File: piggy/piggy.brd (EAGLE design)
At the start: 91.8 x 23 mm, 7 parts, among them J1 M05X2PTH

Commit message: aligned jacks to pot origin
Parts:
- moved CV_JACK 2.54 mm to (39.4, 8.89), turned to 180 degrees
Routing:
- net N$1: track 9.55 -> 14.7 mm
- net LIN: track 84.2 -> 79.5 mm
- net CV_PANEL: track 60.3 -> 62.7 mm
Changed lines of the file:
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@@
 <element name="J1" library="SparkFun" package="AVR_ICSP" value="M05X2PTH" x="81.28" y="19.05" rot="R90"/>
 <element name="IN_JACK" library="erthenvar" package="ERTHENVAR-JACK" value="AUDIO-JACKERTHENVAR" x="71.12" y="8.89" rot="R180"/>
-<element name="CV_JACK" library="erthenvar" package="ERTHENVAR-JACK" value="AUDIO-JACKERTHENVAR" x="39.37" y="6.35"/>
+<element name="CV_JACK" library="erthenvar" package="ERTHENVAR-JACK" value="AUDIO-JACKERTHENVAR" x="39.37" y="8.89" rot="R180"/>
 <element name="OUT_JACK" library="erthenvar" package="ERTHENVAR-JACK" value="AUDIO-JACKERTHENVAR" x="83.82" y="8.89" rot="R180"/>
 <element name="P_GAIN" library="SparkFun" package="PDB12" value="100KB" x="58.42" y="8.89" rot="R90"/>
@@
 <contactref element="J1" pad="9"/>
 <contactref element="P_CV" pad="2"/>
-<wire x1="30.4" y1="8.89" x2="54.356" y2="8.89" width="0.254" layer="1"/>
 <wire x1="54.356" y1="8.89" x2="61.468" y2="15.748" width="0.254" layer="1"/>
 <wire x1="61.468" y1="15.748" x2="72.898" y2="15.748" width="0.254" layer="1"/>
@@
 <wire x1="74.168" y1="14.732" x2="83.312" y2="14.732" width="0.254" layer="16"/>
 <wire x1="83.312" y1="14.732" x2="86.36" y2="17.78" width="0.254" layer="16"/>
+<wire x1="30.4" y1="8.89" x2="32.004" y2="8.89" width="0.254" layer="1"/>
+<wire x1="32.004" y1="8.89" x2="34.036" y2="6.858" width="0.254" layer="1"/>
+<wire x1="34.036" y1="6.858" x2="42.164" y2="6.858" width="0.254" layer="1"/>
+<wire x1="42.164" y1="6.858" x2="42.926" y2="6.096" width="0.254" layer="1"/>
+<wire x1="42.926" y1="6.096" x2="48.006" y2="6.096" width="0.254" layer="1"/>
+<wire x1="48.006" y1="6.096" x2="50.8" y2="8.89" width="0.254" layer="1"/>
+<wire x1="50.8" y1="8.89" x2="54.356" y2="8.89" width="0.254" layer="1"/>
 </signal>
 <signal name="GAIN">
@@
 <contactref element="U$1" pad="X1"/>
 <contactref element="U$1" pad="X2"/>
-<wire x1="6.32" y1="7.33" x2="8.92" y2="7.33" width="0.4064" layer="1"/>
-<wire x1="78.74" y1="20.32" x2="78.74" y2="20.574" width="0.4064" layer="16"/>
-<wire x1="78.74" y1="20.574" x2="77.724" y2="21.59" width="0.254" layer="16"/>
-<wire x1="77.724" y1="21.59" x2="71.374" y2="21.59" width="0.254" layer="16"/>
-<wire x1="71.374" y1="21.59" x2="65.024" y2="15.24" width="0.254" layer="16"/>
-<wire x1="65.024" y1="15.24" x2="65.024" y2="11.684" width="0.254" layer="16"/>
-<wire x1="65.024" y1="11.684" x2="63.754" y2="10.414" width="0.254" layer="16"/>
-<wire x1="63.754" y1="10.414" x2="43.942" y2="10.414" width="0.254" layer="16"/>
-<wire x1="43.942" y1="10.414" x2="40.132" y2="14.224" width="0.254" layer="16"/>
-<wire x1="40.132" y1="14.224" x2="27.178" y2="14.224" width="0.254" layer="16"/>
-<wire x1="27.178" y1="14.224" x2="20.32" y2="7.366" width="0.254" layer="16"/>
-<wire x1="20.32" y1="7.366" x2="8.956" y2="7.366" width="0.254" layer="16"/>
-<wire x1="8.956" y1="7.366" x2="8.92" y2="7.33" width="0.254" layer="16"/>
+<wire x1="6.32" y1="7.33" x2="8.382" y2="7.33" width="0.4064" layer="1"/>
+<wire x1="8.382" y1="7.33" x2="8.92" y2="7.33" width="0.4064" layer="1"/>
+<wire x1="78.74" y1="20.32" x2="78.74" y2="20.574" width="0.254" layer="1"/>
+<wire x1="78.74" y1="20.574" x2="77.724" y2="21.59" width="0.254" layer="1"/>
+<wire x1="77.724" y1="21.59" x2="34.798" y2="21.59" width="0.254" layer="1"/>
+<wire x1="34.798" y1="21.59" x2="20.574" y2="7.366" width="0.254" layer="1"/>
+<wire x1="20.574" y1="7.366" x2="8.418" y2="7.366" width="0.254" layer="1"/>
+<wire x1="8.418" y1="7.366" x2="8.382" y2="7.33" width="0.254" layer="1"/>
 </signal>
 <signal name="EXP">
@@
 <contactref element="CV_JACK" pad="3"/>
 <contactref element="P_CV" pad="3"/>
-<wire x1="30.4" y1="12.64" x2="37.98" y2="12.64" width="0.4064" layer="1"/>
-<wire x1="37.98" y1="12.64" x2="39.37" y2="11.25" width="0.4064" layer="1"/>
+<wire x1="39.37" y1="3.99" x2="39.37" y2="7.62" width="0.254" layer="16"/>
+<wire x1="39.37" y1="7.62" x2="34.29" y2="12.7" width="0.254" layer="16"/>
+<wire x1="34.29" y1="12.7" x2="30.46" y2="12.7" width="0.254" layer="16"/>
+<wire x1="30.46" y1="12.7" x2="30.4" y2="12.64" width="0.254" layer="16"/>
 </signal>
 </signals>

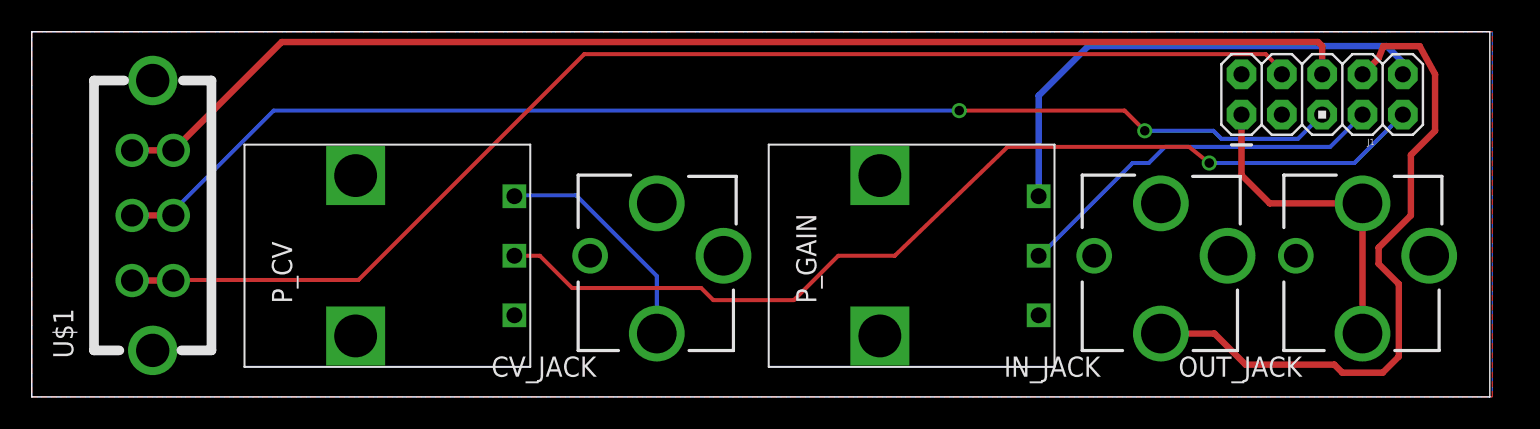
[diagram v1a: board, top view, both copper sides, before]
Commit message: Laid out panel.
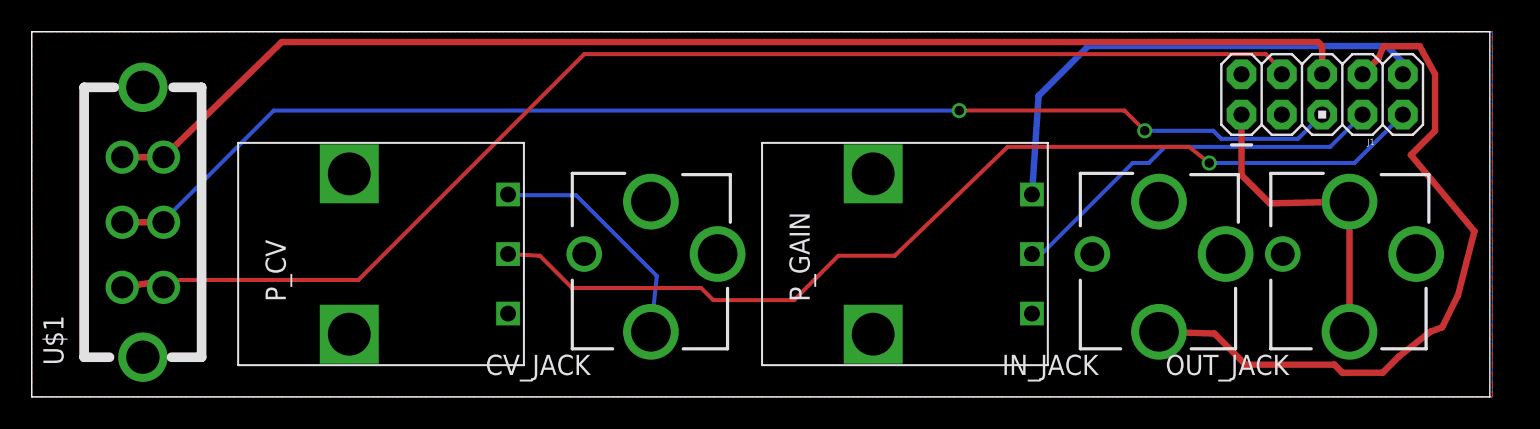
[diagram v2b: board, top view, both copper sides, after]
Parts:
- moved OUT_JACK 0.83 mm to (83.0, 9.00)
- moved U$1 0.75 mm to (7.00, 11.0)
- moved P_GAIN 0.43 mm to (58.0, 9.00)
- moved P_CV 0.41 mm to (25.0, 9.00)
- moved CV_JACK 0.39 mm to (39.0, 9.00)
- moved IN_JACK 0.16 mm to (71.0, 9.00)
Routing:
- net IN: track 42.8 -> 44.8 mm
- net OUT: track 20.4 -> 19.5 mm
- net EXP: track 79.7 -> 80.4 mm
- net INT: track 79.2 -> 79.9 mm
- net LIN: track 79.5 -> 80.1 mm
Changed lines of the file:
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@@
 <setting verticaltext="up"/>
 </settings>
-<grid distance="0.01" unitdist="inch" unit="inch" style="lines" multiple="1" display="yes" altdistance="0.005" altunitdist="inch" altunit="inch"/>
+<grid distance="1" unitdist="mm" unit="mm" style="lines" multiple="1" display="yes" altdistance="0.1" altunitdist="mm" altunit="mm"/>
 <layers>
 <layer number="1" name="Top" color="4" fill="1" visible="yes" active="yes"/>
@@
 <elements>
 <element name="J1" library="SparkFun" package="AVR_ICSP" value="M05X2PTH" x="81.28" y="19.05" rot="R90"/>
-<element name="IN_JACK" library="erthenvar" package="ERTHENVAR-JACK" value="AUDIO-JACKERTHENVAR" x="71.12" y="8.89" rot="R180"/>
-<element name="CV_JACK" library="erthenvar" package="ERTHENVAR-JACK" value="AUDIO-JACKERTHENVAR" x="39.37" y="8.89" rot="R180"/>
-<element name="OUT_JACK" library="erthenvar" package="ERTHENVAR-JACK" value="AUDIO-JACKERTHENVAR" x="83.82" y="8.89" rot="R180"/>
-<element name="P_GAIN" library="SparkFun" package="PDB12" value="100KB" x="58.42" y="8.89" rot="R90"/>
-<element name="P_CV" library="SparkFun" package="PDB12" value="100KB" x="25.4" y="8.89" rot="R90"/>
-<element name="U$1" library="russruss" package="MOUNTAIN_10SL005" value="DPDT" x="7.62" y="11.43" rot="R90"/>
+<element name="IN_JACK" library="erthenvar" package="ERTHENVAR-JACK" value="AUDIO-JACKERTHENVAR" x="71" y="9" rot="R180"/>
+<element name="CV_JACK" library="erthenvar" package="ERTHENVAR-JACK" value="AUDIO-JACKERTHENVAR" x="39" y="9" rot="R180"/>
+<element name="OUT_JACK" library="erthenvar" package="ERTHENVAR-JACK" value="AUDIO-JACKERTHENVAR" x="83" y="9" rot="R180"/>
+<element name="P_GAIN" library="SparkFun" package="PDB12" value="100KB" x="58" y="9" rot="R90"/>
+<element name="P_CV" library="SparkFun" package="PDB12" value="100KB" x="25" y="9" rot="R90"/>
+<element name="U$1" library="russruss" package="MOUNTAIN_10SL005" value="DPDT" x="7" y="11" rot="R90"/>
 </elements>
 <signals>
@@
 <contactref element="J1" pad="10"/>
 <contactref element="P_GAIN" pad="3"/>
-<wire x1="63.42" y1="12.64" x2="63.42" y2="18.97" width="0.4064" layer="16"/>
+<wire x1="63" y1="12.75" x2="63.42" y2="18.97" width="0.4064" layer="16"/>
 <wire x1="63.42" y1="18.97" x2="66.548" y2="22.098" width="0.4064" layer="16"/>
 <wire x1="66.548" y1="22.098" x2="85.344" y2="22.098" width="0.4064" layer="16"/>
@@
 <wire x1="74.168" y1="14.732" x2="83.312" y2="14.732" width="0.254" layer="16"/>
 <wire x1="83.312" y1="14.732" x2="86.36" y2="17.78" width="0.254" layer="16"/>
-<wire x1="30.4" y1="8.89" x2="32.004" y2="8.89" width="0.254" layer="1"/>
+<wire x1="30" y1="9" x2="32.004" y2="8.89" width="0.254" layer="1"/>
 <wire x1="32.004" y1="8.89" x2="34.036" y2="6.858" width="0.254" layer="1"/>
 <wire x1="34.036" y1="6.858" x2="42.164" y2="6.858" width="0.254" layer="1"/>
@@
 <contactref element="J1" pad="7"/>
 <contactref element="P_GAIN" pad="2"/>
-<wire x1="63.42" y1="8.89" x2="63.5" y2="8.89" width="0.254" layer="16"/>
+<wire x1="63" y1="9" x2="63.5" y2="8.89" width="0.254" layer="16"/>
 <wire x1="63.5" y1="8.89" x2="69.342" y2="14.732" width="0.254" layer="16"/>
 <wire x1="69.342" y1="14.732" x2="70.358" y2="14.732" width="0.254" layer="16"/>
@@
 <contactref element="U$1" pad="X1"/>
 <contactref element="U$1" pad="X2"/>
-<wire x1="6.32" y1="7.33" x2="8.382" y2="7.33" width="0.4064" layer="1"/>
-<wire x1="8.382" y1="7.33" x2="8.92" y2="7.33" width="0.4064" layer="1"/>
+<wire x1="5.7" y1="6.9" x2="8.382" y2="7.33" width="0.4064" layer="1"/>
+<wire x1="8.382" y1="7.33" x2="8.3" y2="6.9" width="0.4064" layer="1"/>
 <wire x1="78.74" y1="20.32" x2="78.74" y2="20.574" width="0.254" layer="1"/>
 <wire x1="78.74" y1="20.574" x2="77.724" y2="21.59" width="0.254" layer="1"/>
@@
 <contactref element="U$1" pad="Y1"/>
 <contactref element="U$1" pad="Y2"/>
-<wire x1="6.32" y1="15.53" x2="8.92" y2="15.53" width="0.4064" layer="1"/>
+<wire x1="5.7" y1="15.1" x2="8.3" y2="15.1" width="0.4064" layer="1"/>
 <wire x1="81.28" y1="20.32" x2="81.28" y2="22.098" width="0.4064" layer="1"/>
 <wire x1="81.28" y1="22.098" x2="81.026" y2="22.352" width="0.4064" layer="1"/>
 <wire x1="81.026" y1="22.352" x2="15.742" y2="22.352" width="0.4064" layer="1"/>
-<wire x1="15.742" y1="22.352" x2="8.92" y2="15.53" width="0.4064" layer="1"/>
+<wire x1="15.742" y1="22.352" x2="8.3" y2="15.1" width="0.4064" layer="1"/>
 </signal>
 <signal name="IN">
 <contactref element="J1" pad="8"/>
 <contactref element="IN_JACK" pad="3"/>
-<wire x1="71.12" y1="3.99" x2="74.496" y2="3.99" width="0.4064" layer="1"/>
+<wire x1="71" y1="4.1" x2="74.496" y2="3.99" width="0.4064" layer="1"/>
 <wire x1="74.496" y1="3.99" x2="76.454" y2="2.032" width="0.4064" layer="1"/>
 <wire x1="76.454" y1="2.032" x2="82.042" y2="2.032" width="0.4064" layer="1"/>
@@
 <wire x1="82.55" y1="1.524" x2="85.09" y2="1.524" width="0.4064" layer="1"/>
 <wire x1="85.09" y1="1.524" x2="86.106" y2="2.54" width="0.4064" layer="1"/>
-<wire x1="86.106" y1="2.54" x2="86.106" y2="7.112" width="0.4064" layer="1"/>
-<wire x1="86.106" y1="7.112" x2="84.836" y2="8.382" width="0.4064" layer="1"/>
-<wire x1="84.836" y1="8.382" x2="84.836" y2="9.398" width="0.4064" layer="1"/>
-<wire x1="84.836" y1="9.398" x2="86.868" y2="11.43" width="0.4064" layer="1"/>
-<wire x1="86.868" y1="11.43" x2="86.868" y2="15.24" width="0.4064" layer="1"/>
+<wire x1="86.106" y1="2.54" x2="88.106" y2="4.112" width="0.4064" layer="1"/>
+<wire x1="88.106" y1="4.112" x2="88.836" y2="4.382" width="0.4064" layer="1"/>
+<wire x1="88.836" y1="4.382" x2="89.836" y2="6.398" width="0.4064" layer="1"/>
+<wire x1="89.836" y1="6.398" x2="90.868" y2="10.43" width="0.4064" layer="1"/>
+<wire x1="90.868" y1="10.43" x2="86.868" y2="15.24" width="0.4064" layer="1"/>
 <wire x1="86.868" y1="15.24" x2="88.392" y2="16.764" width="0.4064" layer="1"/>
 <wire x1="88.392" y1="16.764" x2="88.392" y2="20.32" width="0.4064" layer="1"/>
@@
 <contactref element="OUT_JACK" pad="2"/>
 <contactref element="OUT_JACK" pad="3"/>
-<wire x1="83.82" y1="12.19" x2="83.82" y2="3.99" width="0.4064" layer="1"/>
-<wire x1="83.82" y1="12.19" x2="77.98" y2="12.19" width="0.4064" layer="1"/>
+<wire x1="83" y1="12.3" x2="83" y2="4.1" width="0.4064" layer="1"/>
+<wire x1="83" y1="12.3" x2="77.98" y2="12.19" width="0.4064" layer="1"/>
 <wire x1="77.98" y1="12.19" x2="76.2" y2="13.97" width="0.4064" layer="1"/>
 <wire x1="76.2" y1="13.97" x2="76.2" y2="17.78" width="0.4064" layer="1"/>
@@
 <contactref element="U$1" pad="C1"/>
 <contactref element="U$1" pad="C2"/>
-<wire x1="6.32" y1="11.43" x2="8.92" y2="11.43" width="0.4064" layer="1"/>
-<wire x1="8.92" y1="11.43" x2="8.92" y2="11.714" width="0.254" layer="16"/>
+<wire x1="5.7" y1="11" x2="8.3" y2="11" width="0.4064" layer="1"/>
+<wire x1="8.3" y1="11" x2="8.92" y2="11.714" width="0.254" layer="16"/>
 <wire x1="8.92" y1="11.714" x2="15.24" y2="18.034" width="0.254" layer="16"/>
 <wire x1="15.24" y1="18.034" x2="58.42" y2="18.034" width="0.254" layer="16"/>
@@
 <contactref element="CV_JACK" pad="3"/>
 <contactref element="P_CV" pad="3"/>
-<wire x1="39.37" y1="3.99" x2="39.37" y2="7.62" width="0.254" layer="16"/>
+<wire x1="39" y1="4.1" x2="39.37" y2="7.62" width="0.254" layer="16"/>
 <wire x1="39.37" y1="7.62" x2="34.29" y2="12.7" width="0.254" layer="16"/>
 <wire x1="34.29" y1="12.7" x2="30.46" y2="12.7" width="0.254" layer="16"/>
-<wire x1="30.46" y1="12.7" x2="30.4" y2="12.64" width="0.254" layer="16"/>
+<wire x1="30.46" y1="12.7" x2="30" y2="12.75" width="0.254" layer="16"/>
 </signal>
 </signals>

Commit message: hole placement
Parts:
- moved IN_JACK 3.00 mm to (74.0, 9.00)
- moved OUT_JACK 3.00 mm to (86.0, 9.00)
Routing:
- net IN: track 44.8 -> 48.5 mm
- net OUT: track 19.5 -> 22.5 mm
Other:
- board size 91.8 x 23 mm -> 92.8 x 23 mm
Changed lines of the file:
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@@
 <board>
 <plain>
-<wire x1="0" y1="0" x2="91.84" y2="0" width="0" layer="20"/>
-<wire x1="91.84" y1="0" x2="91.84" y2="23" width="0" layer="20"/>
-<wire x1="91.84" y1="23" x2="0" y2="23" width="0" layer="20"/>
+<wire x1="0" y1="0" x2="92.84" y2="0" width="0" layer="20"/>
+<wire x1="92.84" y1="0" x2="92.84" y2="23" width="0" layer="20"/>
+<wire x1="92.84" y1="23" x2="0" y2="23" width="0" layer="20"/>
 <wire x1="0" y1="23" x2="0" y2="0" width="0" layer="20"/>
 </plain>
@@
 <elements>
 <element name="J1" library="SparkFun" package="AVR_ICSP" value="M05X2PTH" x="81.28" y="19.05" rot="R90"/>
-<element name="IN_JACK" library="erthenvar" package="ERTHENVAR-JACK" value="AUDIO-JACKERTHENVAR" x="71" y="9" rot="R180"/>
+<element name="IN_JACK" library="erthenvar" package="ERTHENVAR-JACK" value="AUDIO-JACKERTHENVAR" x="74" y="9" rot="R180"/>
 <element name="CV_JACK" library="erthenvar" package="ERTHENVAR-JACK" value="AUDIO-JACKERTHENVAR" x="39" y="9" rot="R180"/>
-<element name="OUT_JACK" library="erthenvar" package="ERTHENVAR-JACK" value="AUDIO-JACKERTHENVAR" x="83" y="9" rot="R180"/>
+<element name="OUT_JACK" library="erthenvar" package="ERTHENVAR-JACK" value="AUDIO-JACKERTHENVAR" x="86" y="9" rot="R180"/>
 <element name="P_GAIN" library="SparkFun" package="PDB12" value="100KB" x="58" y="9" rot="R90"/>
 <element name="P_CV" library="SparkFun" package="PDB12" value="100KB" x="25" y="9" rot="R90"/>
@@
 <vertex x="0" y="23"/>
 <vertex x="0" y="0"/>
-<vertex x="92" y="0"/>
-<vertex x="92" y="23"/>
+<vertex x="93" y="0"/>
+<vertex x="93" y="23"/>
 </polygon>
 <polygon width="0.4064" layer="16">
 <vertex x="0" y="23"/>
-<vertex x="92" y="23"/>
-<vertex x="92" y="0"/>
+<vertex x="93" y="23"/>
+<vertex x="93" y="0"/>
 <vertex x="0" y="0"/>
 </polygon>
@@
 <contactref element="J1" pad="8"/>
 <contactref element="IN_JACK" pad="3"/>
-<wire x1="71" y1="4.1" x2="74.496" y2="3.99" width="0.4064" layer="1"/>
-<wire x1="74.496" y1="3.99" x2="76.454" y2="2.032" width="0.4064" layer="1"/>
-<wire x1="76.454" y1="2.032" x2="82.042" y2="2.032" width="0.4064" layer="1"/>
-<wire x1="82.042" y1="2.032" x2="82.55" y2="1.524" width="0.4064" layer="1"/>
-<wire x1="82.55" y1="1.524" x2="85.09" y2="1.524" width="0.4064" layer="1"/>
-<wire x1="85.09" y1="1.524" x2="86.106" y2="2.54" width="0.4064" layer="1"/>
-<wire x1="86.106" y1="2.54" x2="88.106" y2="4.112" width="0.4064" layer="1"/>
-<wire x1="88.106" y1="4.112" x2="88.836" y2="4.382" width="0.4064" layer="1"/>
-<wire x1="88.836" y1="4.382" x2="89.836" y2="6.398" width="0.4064" layer="1"/>
-<wire x1="89.836" y1="6.398" x2="90.868" y2="10.43" width="0.4064" layer="1"/>
-<wire x1="90.868" y1="10.43" x2="86.868" y2="15.24" width="0.4064" layer="1"/>
-<wire x1="86.868" y1="15.24" x2="88.392" y2="16.764" width="0.4064" layer="1"/>
-<wire x1="88.392" y1="16.764" x2="88.392" y2="20.32" width="0.4064" layer="1"/>
-<wire x1="88.392" y1="20.32" x2="87.422" y2="22.09" width="0.4064" layer="1"/>
-<wire x1="87.422" y1="22.09" x2="85.136" y2="22.09" width="0.4064" layer="1"/>
-<wire x1="85.136" y1="22.09" x2="84.836" y2="21.336" width="0.4064" layer="1"/>
-<wire x1="84.836" y1="21.336" x2="83.82" y2="20.32" width="0.4064" layer="1"/>
+<wire x1="83.82" y1="20.32" x2="83.82" y2="20.82" width="0.4064" layer="1"/>
+<wire x1="83.82" y1="20.82" x2="85" y2="22" width="0.4064" layer="1"/>
+<wire x1="85" y1="22" x2="90" y2="22" width="0.4064" layer="1"/>
+<wire x1="90" y1="22" x2="91" y2="21" width="0.4064" layer="1"/>
+<wire x1="91" y1="21" x2="91" y2="14" width="0.4064" layer="1"/>
+<wire x1="91" y1="14" x2="87" y2="10" width="0.4064" layer="1"/>
+<wire x1="87" y1="10" x2="87" y2="7" width="0.4064" layer="1"/>
+<wire x1="87" y1="7" x2="89" y2="5" width="0.4064" layer="1"/>
+<wire x1="89" y1="5" x2="89" y2="2" width="0.4064" layer="1"/>
+<wire x1="89" y1="2" x2="88" y2="1" width="0.4064" layer="1"/>
+<wire x1="88" y1="1" x2="74.1" y2="1" width="0.4064" layer="1"/>
+<wire x1="74.1" y1="1" x2="74" y2="4.1" width="0.4064" layer="1"/>
 </signal>
 <signal name="OUT">
@@
 <contactref element="OUT_JACK" pad="2"/>
 <contactref element="OUT_JACK" pad="3"/>
-<wire x1="83" y1="12.3" x2="83" y2="4.1" width="0.4064" layer="1"/>
-<wire x1="83" y1="12.3" x2="77.98" y2="12.19" width="0.4064" layer="1"/>
+<wire x1="86" y1="12.3" x2="86" y2="4.1" width="0.4064" layer="1"/>
+<wire x1="86" y1="12.3" x2="77.98" y2="12.19" width="0.4064" layer="1"/>
 <wire x1="77.98" y1="12.19" x2="76.2" y2="13.97" width="0.4064" layer="1"/>
 <wire x1="76.2" y1="13.97" x2="76.2" y2="17.78" width="0.4064" layer="1"/>

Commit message: fixed footprint/front panel
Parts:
- moved P_CV 5.00 mm to (20.0, 9.00)
- moved P_GAIN 5.00 mm to (53.0, 9.00)
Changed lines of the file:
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@@
 <element name="CV_JACK" library="erthenvar" package="ERTHENVAR-JACK" value="AUDIO-JACKERTHENVAR" x="39" y="9" rot="R180"/>
 <element name="OUT_JACK" library="erthenvar" package="ERTHENVAR-JACK" value="AUDIO-JACKERTHENVAR" x="86" y="9" rot="R180"/>
-<element name="P_GAIN" library="SparkFun" package="PDB12" value="100KB" x="58" y="9" rot="R90"/>
-<element name="P_CV" library="SparkFun" package="PDB12" value="100KB" x="25" y="9" rot="R90"/>
+<element name="P_GAIN" library="SparkFun" package="PDB12" value="100KB" x="53" y="9" rot="R90"/>
+<element name="P_CV" library="SparkFun" package="PDB12" value="100KB" x="20" y="9" rot="R90"/>
 <element name="U$1" library="russruss" package="MOUNTAIN_10SL005" value="DPDT" x="7" y="11" rot="R90"/>
 </elements>
